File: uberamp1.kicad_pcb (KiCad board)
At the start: 2 copper layers, 152.1 x 125.2 mm, 254 parts, among them IC1 TPA3255, IC2 TPA3255, J1 Conn_01x04, J2 Conn_01x04, U1 Opamp_Dual, U2 Opamp_Dual, U3 Opamp_Dual, U4 Opamp_Dual, U5 Opamp_Dual, U6 Opamp_Dual, U7 Opamp_Dual, U8 Opamp_Dual

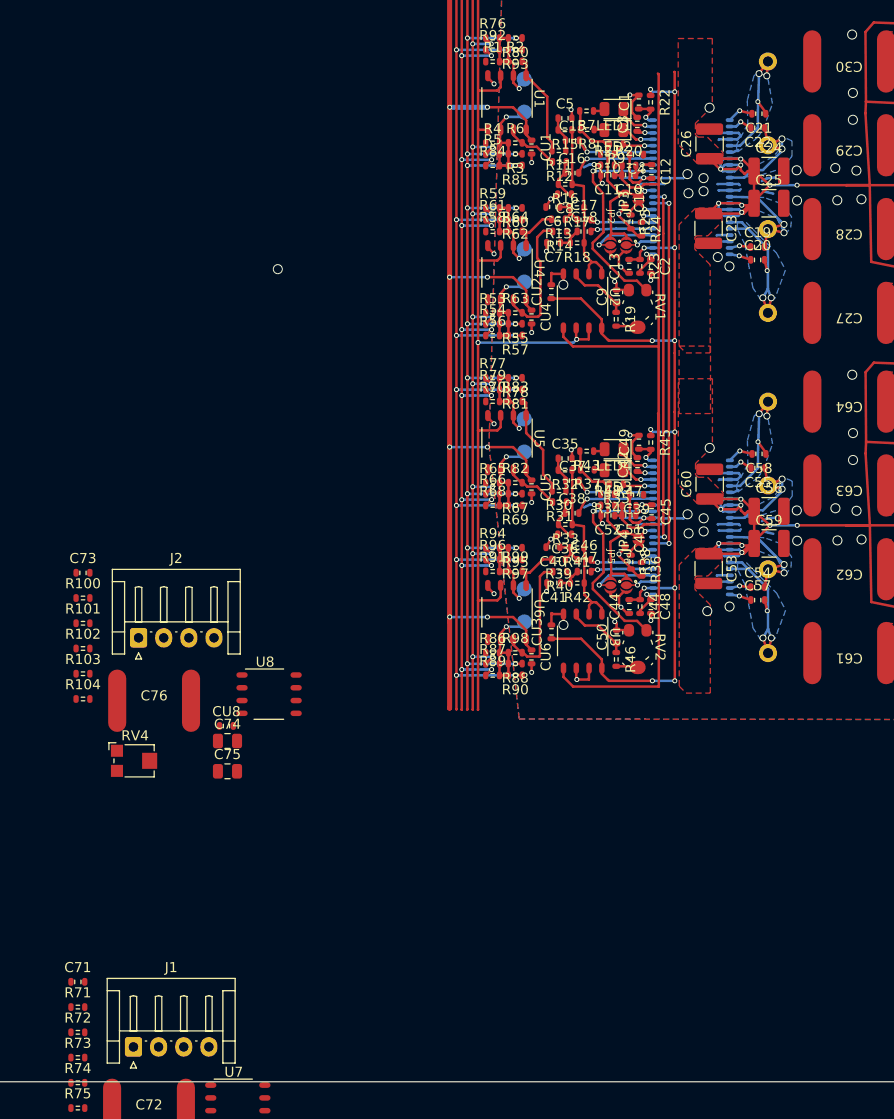
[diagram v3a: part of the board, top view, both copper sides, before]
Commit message: add bypass caps to fakegnd
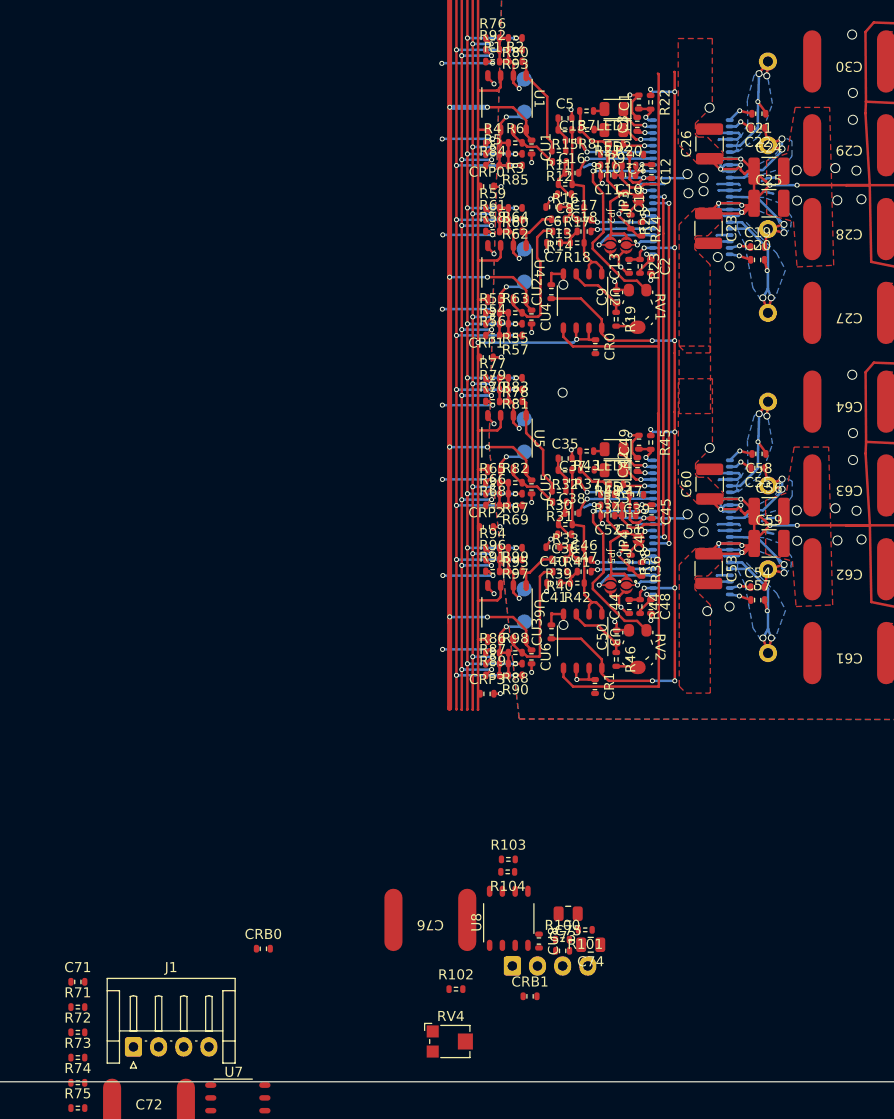
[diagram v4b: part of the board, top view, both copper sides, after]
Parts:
- added CR0: 10u, invendelirium_audio:C_0603, F.Cu at (90.5, 70.4)
- added CR1: 10u, invendelirium_audio:C_0603, F.Cu at (90.5, 104.2)
- added CRB0: 10u, invendelirium_audio:C_0603, F.Cu at (57.5, 130.2)
- added CRB1: 10u, invendelirium_audio:C_0603, F.Cu at (84.0, 134.9)
- added CRP0: 10u, invendelirium_audio:C_0603, F.Cu at (79.8, 54.4)
- added CRP1: 10u, invendelirium_audio:C_0603, F.Cu at (79.7, 71.4)
- added CRP2: 10u, invendelirium_audio:C_0603, F.Cu at (79.7, 88.3)
- added CRP3: 10u, invendelirium_audio:C_0603, F.Cu at (79.8, 104.9)
- J2: moved to B.Cu
- moved C73 60.7 mm to (87.3, 130.4)
- moved R100 58.5 mm to (87.3, 129.3)
- moved R101 58.5 mm to (89.5, 128.3), turned to 180 degrees
- moved R102 50.2 mm to (76.7, 134.2)
- moved J2 49.5 mm to (82.3, 131.9)
- moved R103 46.1 mm to (81.9, 121.3)
- moved R104 45.6 mm to (81.8, 122.6), turned to 180 degrees
- moved RV4 42.0 mm to (76.2, 139.4)
- moved C74 41.4 mm to (90.1, 129.8), turned to 180 degrees
- moved CU8 37.7 mm to (84.9, 129.5), turned to -90 degrees
- moved C75 36.7 mm to (87.8, 126.7), turned to 180 degrees
- moved C76 35.1 mm to (74.1, 127.4), turned to 180 degrees
- moved U8 32.6 mm to (81.9, 127.2), turned to 90 degrees
- renumbered s1 to s0, s0 to s1, s3 to s2, s2 to s3, s5 to s4, s4 to s5, s7 to s6, s6 to s7
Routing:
- net /preamp3/in0: track 0.00 -> 5.87 mm, vias 0 -> 2
- net /preamp2/in0: track 0.00 -> 5.86 mm, vias 0 -> 2
- net /preamp0/in1: track 0.00 -> 5.85 mm, vias 0 -> 2
- net /preamp1/in1: track 0.00 -> 5.83 mm, vias 0 -> 2
- net /preamp0/in0: track 0.00 -> 5.81 mm, vias 0 -> 2
- net /preamp3/in1: track 0.00 -> 5.78 mm, vias 0 -> 2
- net /preamp2/in1: track 0.00 -> 5.77 mm, vias 0 -> 2
- net /preamp1/in0: track 0.00 -> 5.76 mm, vias 0 -> 2
- net /inputref: track 109.1 -> 112.7 mm
- net GND: track 116.3 -> 119.2 mm, vias 65 -> 69
- net /~fb1: track 131.6 -> 132.7 mm
- net /poweramp1/input_ref: track 3.49 -> 4.10 mm

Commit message: update feedbass components
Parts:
- C72, C76: value 1uF -> 0.33uF; footprint invendelirium_audio:CB052D0105KBC film cap -> Capacitor_SMD:C_1206_3216Metric
- RV3: value 10k -> 1k; footprint Potentiometer_SMD:Potentiometer_Bourns_TC33X_Vertical -> invendelirium_audio:PV37X
- RV4: value 10k -> 1k; footprint Potentiometer_SMD:Potentiometer_Bourns_TC33X_Vertical -> invendelirium_audio:PV37X; moved to B.Cu
- moved RV4 15.6 mm to (82.1, 125.0), turned to 180 degrees
- moved R103 0.83 mm to (81.8, 120.5)

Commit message: fix feedbass filter
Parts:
- R102, R74: value 75 -> 240
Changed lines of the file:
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@@
         (effects (font (size 1 1) (thickness 0.15)))
     )
-    (fp_text value "75" (at 0 1.43) (layer "F.Fab")
+    (fp_text value "240" (at 0 1.43) (layer "F.Fab")
         (effects (font (size 1 1) (thickness 0.15)))
     )
@@
         (effects (font (size 1 1) (thickness 0.15)))
     )
-    (fp_text value "75" (at 0 1.43) (layer "F.Fab")
-        (effects (font (size 1 1) (thickness 0.15)))
-    )
+    (fp_text value "240" (at 0 1.43) (layer "F.Fab")
+        (effects (font (size 1 1) (thickness 0.15)))
+    )
